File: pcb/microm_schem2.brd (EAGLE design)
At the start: 101.6 x 81.3 mm, 83 parts, among them Q1 16 MHz

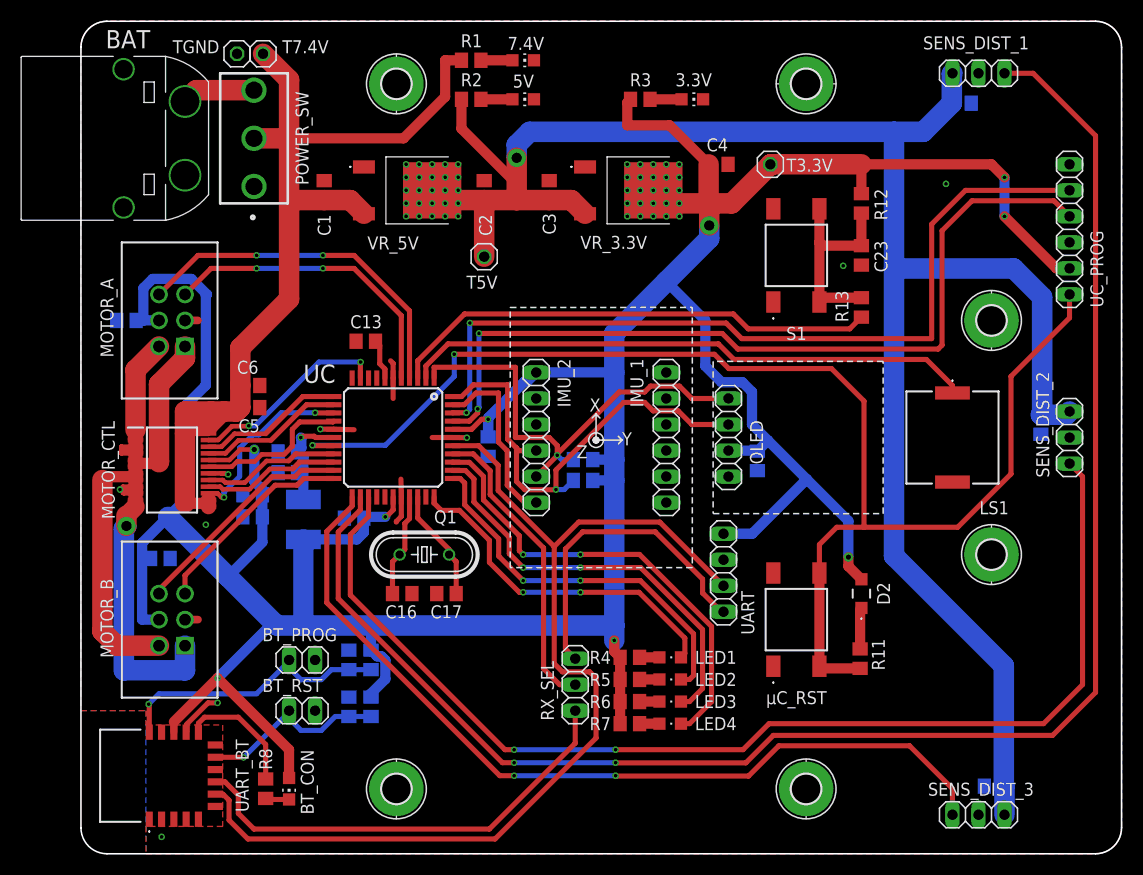
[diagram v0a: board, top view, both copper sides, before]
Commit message: Add GPIO header for remaining pins.
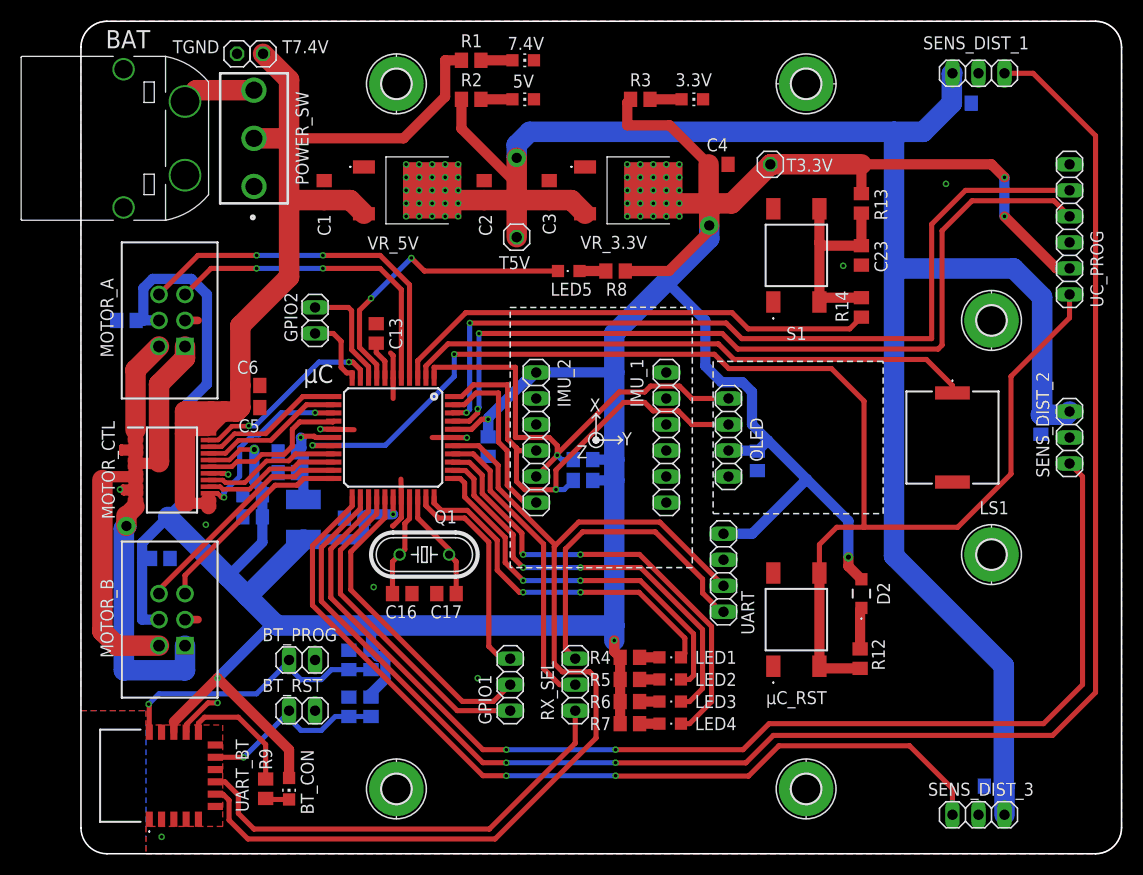
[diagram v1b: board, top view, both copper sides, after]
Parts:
- added GPIO1: (no value), pinhead:1X03
- added GPIO2: (no value), pinhead:1X02
- added LED5: red, 2mA, 2.1V, led:CHIPLED_0805
- added R16: 10kΩ, rcl:R0805
- R11: value 10kΩ -> 2.2kΩ
- R13: value 1kΩ -> 10kΩ
- R14: value 10kΩ -> 1kΩ
- R8: value 180Ω -> 680Ω
- R9: value 2.2kΩ -> 180Ω
- moved R8 61.0 mm to (52.2, 56.9), turned to 180 degrees
- moved R14 59.0 mm to (76.2, 53.3), flipped to the top, turned to 270 degrees
- moved R12 44.5 mm to (76.1, 19.1)
- moved R9 43.2 mm to (18.0, 6.35), flipped to the top, turned to 270 degrees
- moved R11 33.3 mm to (49.0, 38.5), flipped to the bottom, turned to 0 degrees
- moved R13 10.2 mm to (76.2, 63.5), turned to 90 degrees
- moved R15 4.57 mm to (28.3, 18.9)
- moved T5V 3.70 mm to (42.5, 60.2)
- moved R10 2.03 mm to (49.0, 36.4)
- moved C13 1.27 mm to (28.8, 50.8), turned to 270 degrees
- renumbered UC to μC
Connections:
- new net GPIO_11: GPIO2.2, μC.11
- new net GPIO_26: GPIO1.1, μC.26
- new net GPIO_27: GPIO1.2, μC.27
- new net GPIO_32: GPIO1.3, μC.32
- new net GPIO_9: GPIO2.1, μC.9
- new net LED5: LED5.C, μC.8
- new net N$63: LED5.A, R8.2
- net +3V3: now also R11.1, R13.2, R16.2, R8.1; no longer R12.2, R14.2, R9.1
- net BT_PROG: now also R15.1; no longer R14.1
- net BT_RESET: now also R16.1; no longer R15.1
- net BT_STATUS: now also R9.1; no longer R8.1
- net BUTTON1: now also R14.2; no longer R13.2
- net I2C_SCL: now also R10.2; no longer R9.2
- net I2C_SDA: now also R11.2; no longer R10.2
- net MCLR: now also R12.1; no longer R11.1
- net N$1: now also R9.2; no longer R8.2
- net N$6: now also R14.1; no longer R12.1
- net N$7: now also R12.2; no longer R11.2
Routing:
- net GPIO_26: track 0.00 -> 32.2 mm
- net GPIO_27: track 0.00 -> 31.2 mm
- net LED5: track 0.00 -> 29.4 mm, vias 0 -> 2
- net GPIO_32: track 0.00 -> 21.2 mm
- net GPIO_9: track 0.00 -> 11.0 mm
- net +3V3: track 375.6 -> 385.5 mm
- net GPIO_11: track 0.00 -> 7.21 mm
- net SENS_DIST_2: track 112.8 -> 115.6 mm
- net N$63: track 0.00 -> 2.57 mm
- net SENS_DIST_1: track 160.0 -> 162.5 mm
- net SENS_DIST_3: track 85.0 -> 87.1 mm
- net +5V: track 187.3 -> 185.3 mm
- net MA_ENC_A: track 34.8 -> 36.3 mm
- net MA_ENC_B: track 30.2 -> 31.7 mm
- net GND: track 35.0 -> 36.4 mm, vias 9 -> 11

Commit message: Finalize traces.
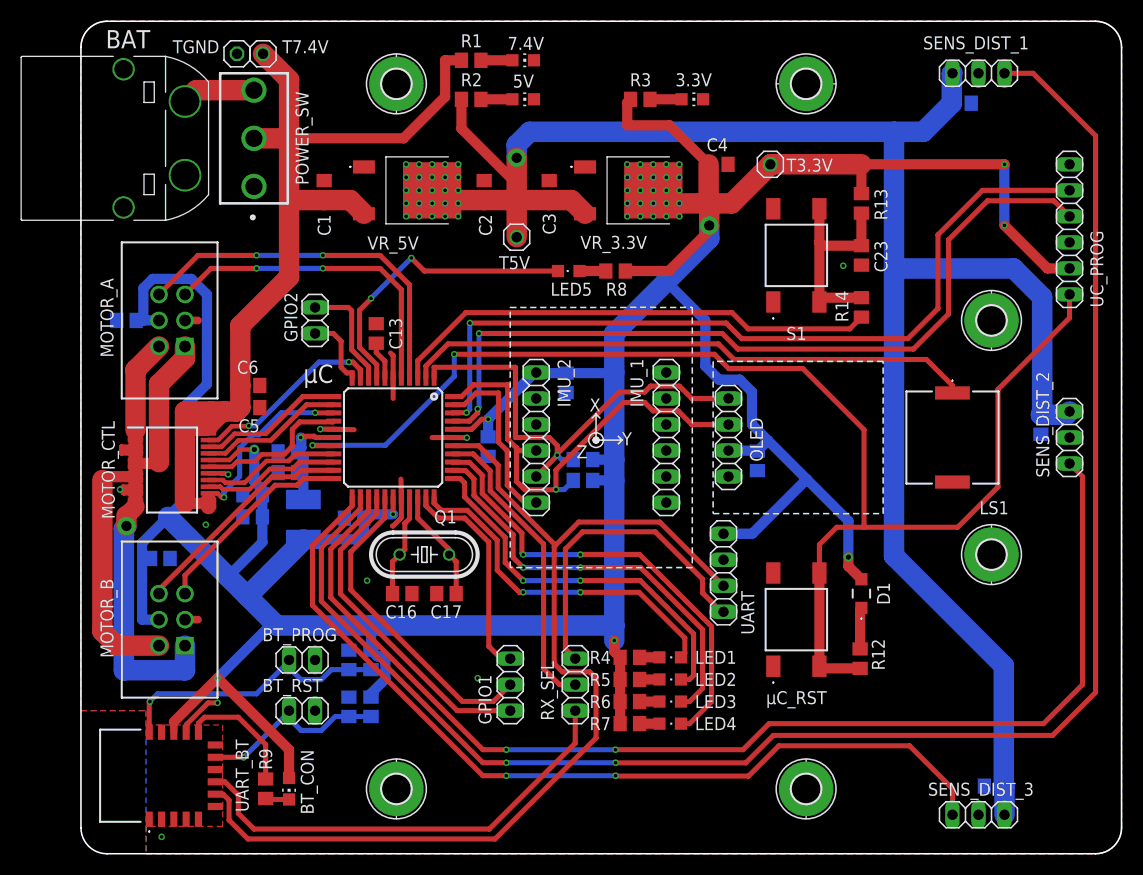
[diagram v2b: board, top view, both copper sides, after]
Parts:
- added C25: 1uF, rcl:C0805
- renumbered D2 to D1
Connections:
- net +3V3: now also C25.1
- net GND: now also C25.2
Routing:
- net PG_EC3: track 82.0 -> 79.7 mm
- net PG_ED3: track 82.1 -> 79.7 mm
- net MCLR: track 132.5 -> 130.9 mm
- net GND: vias 11 -> 10

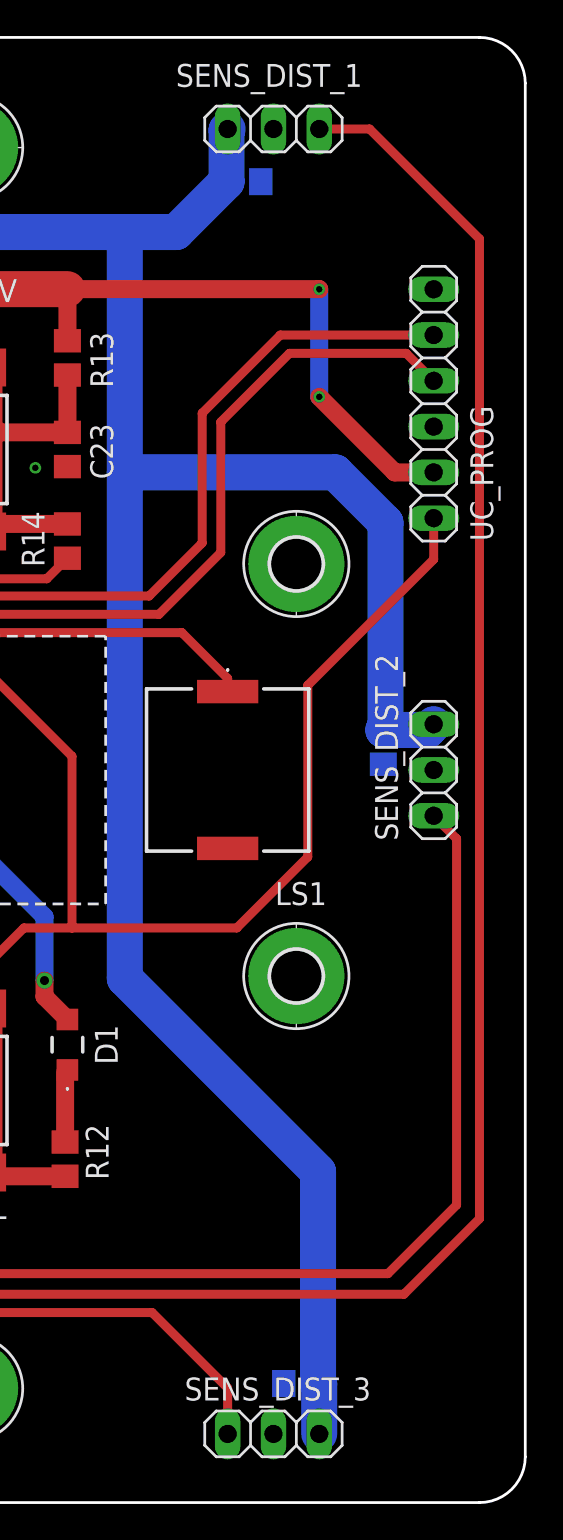
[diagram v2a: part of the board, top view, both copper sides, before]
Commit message: Add TUM logo and update values.
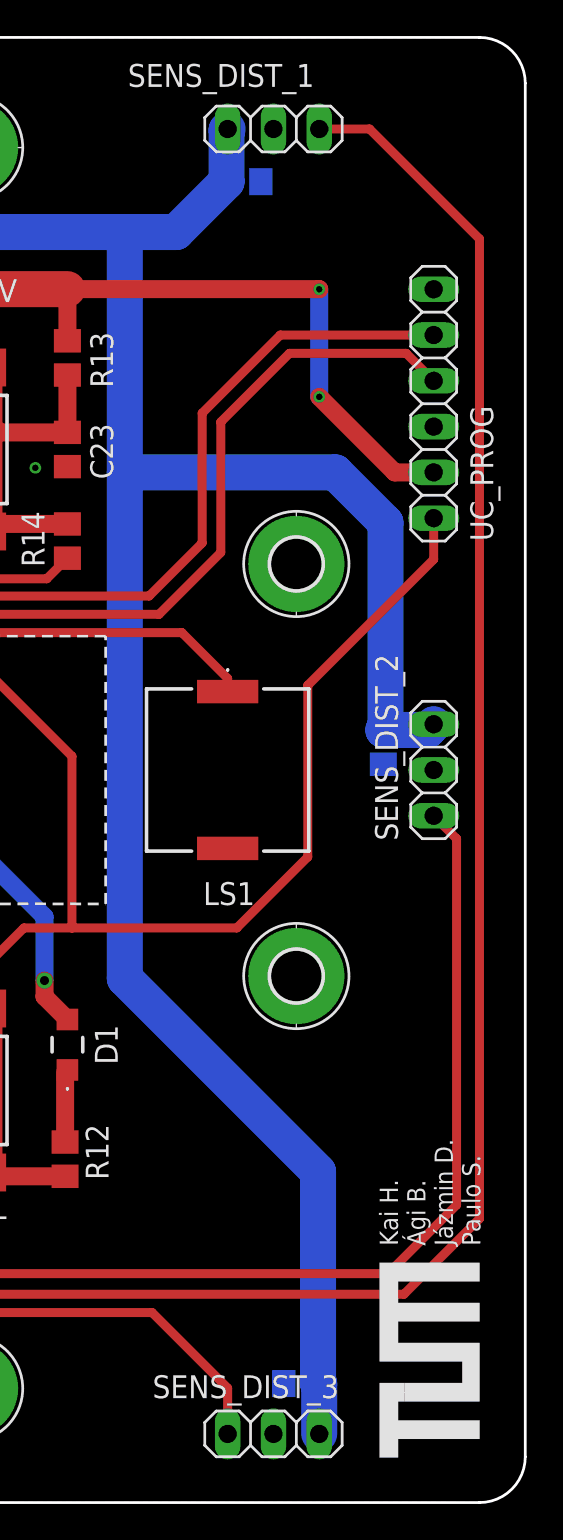
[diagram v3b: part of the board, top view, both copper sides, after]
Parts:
- C13: value 10uF, 10-20V, low-esr -> 10uF, 10-20V, low-esr, tantalum
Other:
- board text added: "Kai H. Ági B. Jázmin D. Paulo S."
